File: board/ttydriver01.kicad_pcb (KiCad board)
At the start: 2 copper layers, 119.4 x 74.9 mm, 55 parts, among them J1 PRINTER JACK, J2 KEYBOARD JACK, J3 MOTOR CTL RELAY JACK, P1 CONN_01X02, SW1 Switch_SPDT, SW2 Button_SPDT, T1 Coilcraft-FA2469-AL, U1 NE555, U2 AP2553W6, U3 CP2102-breakout, U4 CPC1510G, U5 IE0524S, U6 CPC1510G, U7 CPC1510G, U8 IE0512S, U9 FDS4559

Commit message: Fabbable board, but BOM not entirely filled in
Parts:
- added REF1: MountingHole_2.7mm_M2.5, Mounting_Holes:MountingHole_2.7mm_M2.5, F.Cu at (61.0, 80.8)
- added REF2: MountingHole_2.7mm_M2.5, Mounting_Holes:MountingHole_2.7mm_M2.5, F.Cu at (61.0, 148.8)
- added REF3: MountingHole_2.7mm_M2.5, Mounting_Holes:MountingHole_2.7mm_M2.5, F.Cu at (170.2, 80.8)
- added REF4: MountingHole_2.7mm_M2.5, Mounting_Holes:MountingHole_2.7mm_M2.5, F.Cu at (170.2, 148.8)
- added REF5: Fiducial_classic_Small_SilkscreenTop_Type1, Fiducials:Fiducial_classic_Small_SilkscreenTop_Type1, F.Cu at (69.1, 80.3)
- added W4: TEST_1P, Connect:PINTST, F.Cu at (135.1, 144.3)
- C9: value 1000uf -> 220uf
- moved U2 4.10 mm to (154.4, 92.2)
- moved C6 3.39 mm to (137.2, 137.4), turned to 180 degrees
- moved SW2 0.76 mm to (169.2, 104.4)
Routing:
- net GND: track 0.00 -> 373.6 mm, vias 0 -> 1
- net VCC: track 0.00 -> 237.5 mm
- net /HVNEG: track 0.00 -> 143.4 mm
- net Net-(J3-PadT): track 2.54 -> 115.6 mm, vias 0 -> 1
- net Net-(J2-PadS): track 0.00 -> 109.7 mm
- net Net-(C3-Pad1): track 0.00 -> 99.0 mm
- net /ENABLE: track 0.00 -> 81.9 mm, vias 0 -> 1
- net Net-(SW1-Pad2): track 0.40 -> 81.8 mm
- net Net-(SW2-Pad3): track 0.00 -> 70.1 mm
- net Net-(D8-Pad1): track 0.00 -> 60.7 mm
- net /RxD: track 0.00 -> 57.7 mm
- net Net-(D12-Pad2): track 0.00 -> 57.1 mm, vias 0 -> 1
- net Net-(R16-Pad1): track 0.00 -> 56.1 mm, vias 0 -> 2
- net /TxD: track 0.00 -> 52.0 mm, vias 0 -> 1
- net Net-(R13-Pad2): track 0.00 -> 50.3 mm, vias 0 -> 1
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- removed copper zone on B.Cu, net GND
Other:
- net class Default: clearance 0.2 -> 0.14; trace_width 0.25 -> 0.45
- net class HV added: clearance 0.5, trace_width 1, via_dia 0.6, via_drill 0.4
- net class PWR: clearance 0.6 -> 0.14
- rule trace_clearance: 0.2 -> 0.14

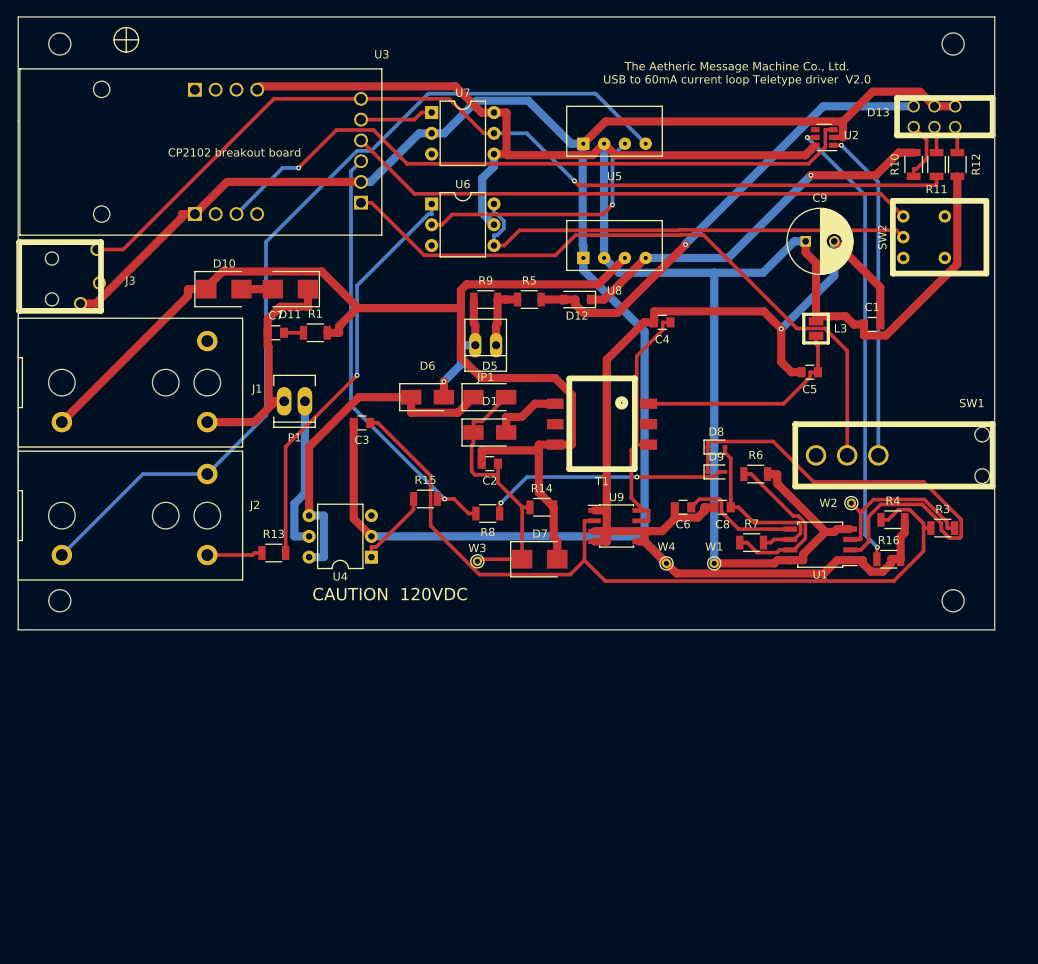
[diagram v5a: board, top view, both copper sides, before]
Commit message: Move components slightly to improve layout
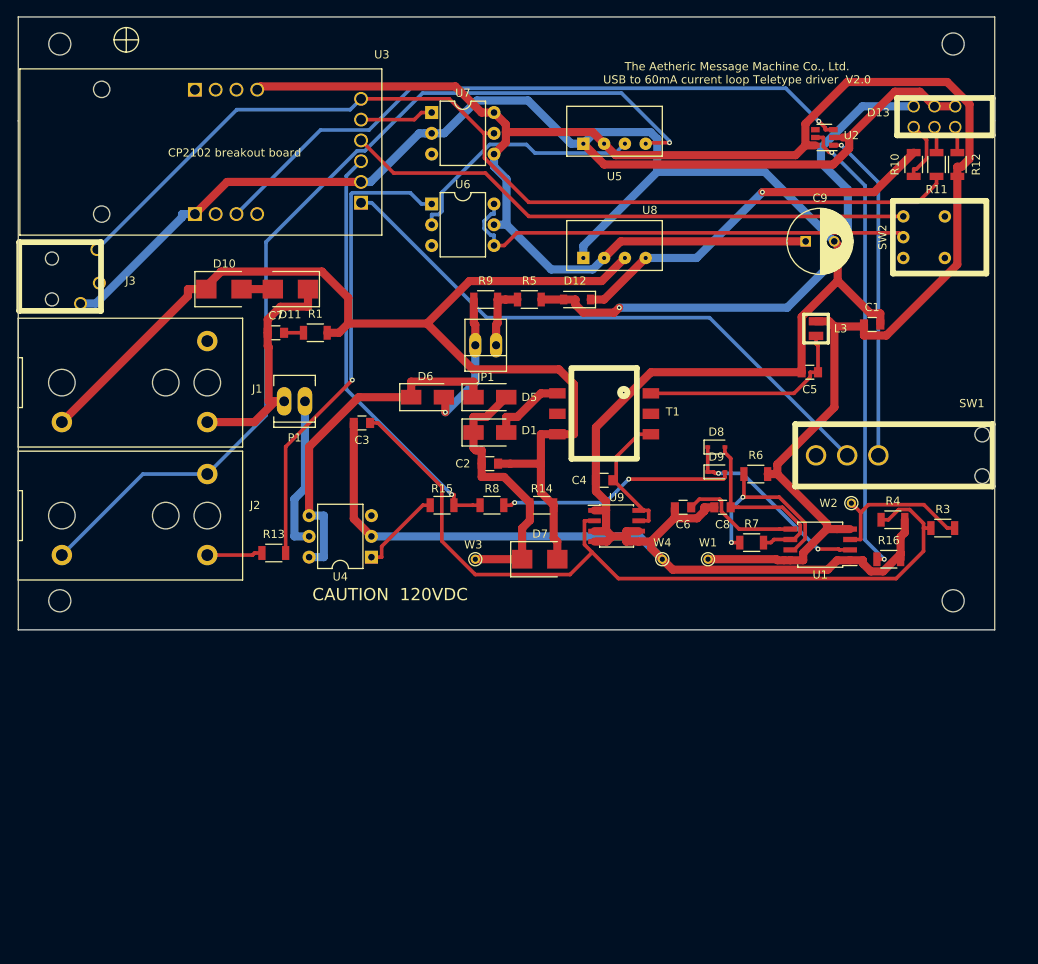
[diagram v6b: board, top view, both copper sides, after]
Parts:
- moved C4 20.6 mm to (127.5, 134.1)
- moved R15 2.17 mm to (107.7, 137.2)
- moved T1 1.30 mm to (127.5, 126.0)
- moved R8 1.14 mm to (113.8, 137.2)
- moved W1 0.92 mm to (140.2, 143.8)
- moved W4 0.72 mm to (134.6, 143.8)
- moved W3 0.36 mm to (111.8, 143.8)
- moved R14 0.25 mm to (119.9, 137.2)
- turned C2 to 0 degrees
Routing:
- net Net-(D8-Pad1): track 60.7 -> 24.4 mm, vias 0 -> 2
- net Net-(C4-Pad1): track 31.3 -> 17.5 mm
- net Net-(D12-Pad2): track 57.1 -> 68.8 mm
- net Net-(SW1-Pad2): track 81.8 -> 72.2 mm
- net VCC: track 237.5 -> 247.1 mm
- net GND: track 373.6 -> 364.6 mm, vias 1 -> 0
- net Net-(R13-Pad2): track 50.3 -> 57.8 mm
- net Net-(J2-PadS): track 109.7 -> 115.7 mm, vias 0 -> 1
- net Net-(J3-PadT): track 115.6 -> 120.3 mm, vias 1 -> 0
- net /HVNEG: track 143.4 -> 140.7 mm
- net Net-(D6-Pad2): track 14.6 -> 17.3 mm
- net Net-(R6-Pad1): track 21.1 -> 23.3 mm, vias 0 -> 2
- net Net-(D9-Pad2): track 30.4 -> 29.1 mm
- net Net-(D5-Pad1): track 42.4 -> 43.5 mm
- net Net-(R15-Pad1): track 9.59 -> 10.6 mm
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
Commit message: Untested but fabbable board
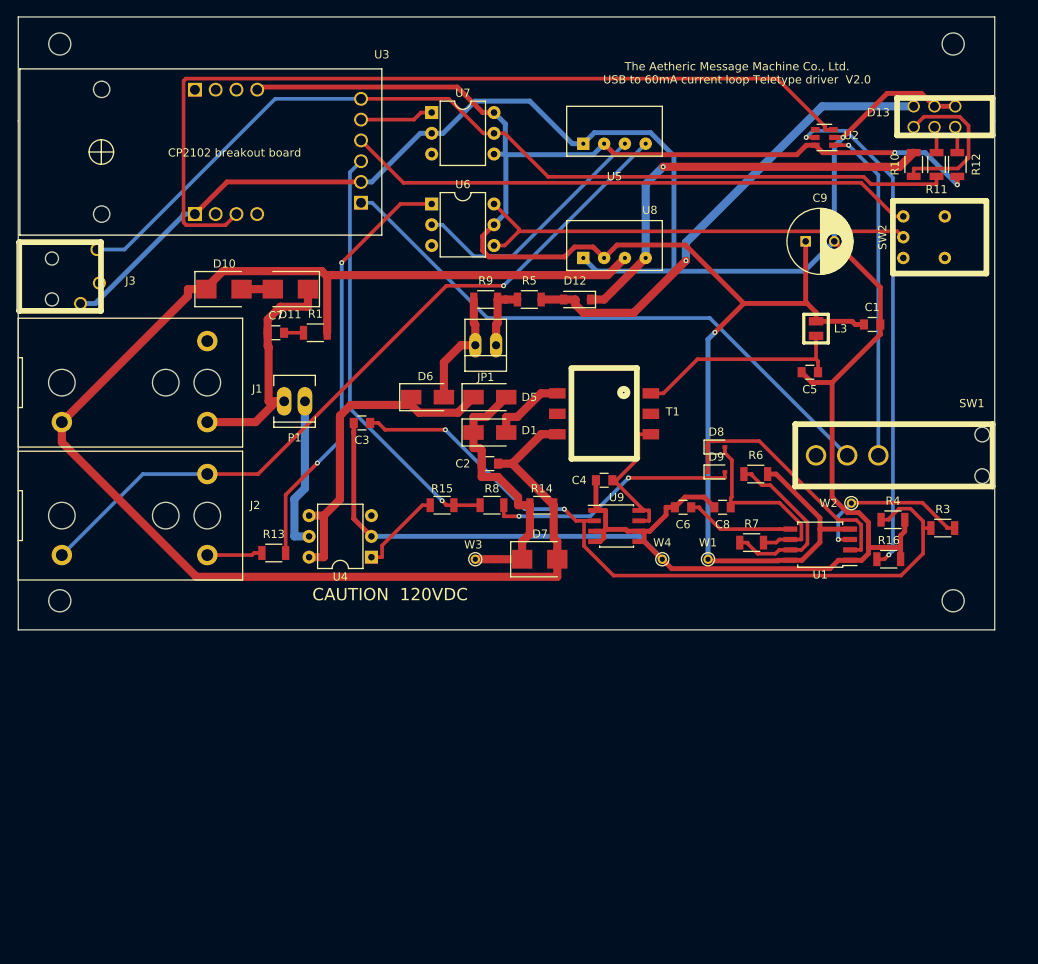
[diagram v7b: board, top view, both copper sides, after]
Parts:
- moved REF5 14.1 mm to (66.0, 94.0)
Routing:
- net /HVNEG: track 140.7 -> 180.0 mm
- net GND: track 364.6 -> 333.8 mm, vias 0 -> 1
- net /ENABLE: track 81.6 -> 106.9 mm, vias 1 -> 0
- net Net-(J2-PadS): track 115.7 -> 92.2 mm
- net VCC: track 247.1 -> 234.2 mm, vias 0 -> 3
- net Net-(D13-Pad6): track 7.52 -> 19.8 mm
- net Net-(D12-Pad2): track 68.8 -> 58.3 mm
- net Net-(C3-Pad1): track 99.2 -> 90.9 mm, vias 0 -> 2
- net Net-(D8-Pad1): track 24.4 -> 31.2 mm, vias 2 -> 0
- net Net-(R16-Pad1): track 56.7 -> 62.5 mm
- net Net-(R13-Pad2): track 57.8 -> 52.3 mm, vias 1 -> 2
- net Net-(D12-Pad1): track 46.9 -> 52.2 mm
- net Net-(J3-PadT): track 120.3 -> 115.6 mm
- net Net-(D5-Pad1): track 43.5 -> 40.7 mm
- net Net-(D6-Pad2): track 17.3 -> 14.6 mm, vias 1 -> 0
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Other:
- net class Default: clearance 0.14 -> 0.28
- net class PWR: clearance 0.14 -> 0.28; trace_width 1 -> 0.6
- rule trace_clearance: 0.14 -> 0.28
